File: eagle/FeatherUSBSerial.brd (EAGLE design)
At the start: 50.8 x 22.9 mm, 14 parts, among them U1 FT232RLSSOP

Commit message: Added Big Buttons
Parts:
- added U$3, U$4: TL3300CFXXXQ, S2JLibrary:12MM_TACTILE
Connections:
- new net !RST: MS1.1, U$4.1, U$4.2
- new net MD: MS1.3, U$3.1, U$3.2
- net GND: now also U$3.3, U$3.4, U$4.3, U$4.4
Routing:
- net !RST: track 0.00 -> 52.5 mm, vias 0 -> 2
- net MD: track 0.00 -> 36.3 mm, vias 0 -> 2
- net RX: track 38.1 -> 45.1 mm
- net TX: track 38.0 -> 41.2 mm
- net VCCIO: track 25.6 -> 26.6 mm
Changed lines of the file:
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@@
 <?xml version="1.0" encoding="utf-8"?>
 <!DOCTYPE eagle SYSTEM "eagle.dtd">
-<eagle version="9.2.2">
+<eagle version="9.3.0">
 <drawing>
 <settings>
@@
 <setting verticaltext="up"/>
 </settings>
-<grid distance="0.1" unitdist="inch" unit="inch" style="lines" multiple="1" display="no" altdistance="0.025" altunitdist="inch" altunit="inch"/>
+<grid distance="25" unitdist="mil" unit="mil" style="lines" multiple="1" display="yes" altdistance="12.5" altunitdist="mil" altunit="mil"/>
 <layers>
 <layer number="1" name="Top" color="4" fill="1" visible="yes" active="yes"/>
@@
 <text x="43.815" y="19.431" size="0.8128" layer="21" font="vector" ratio="12">SDA</text>
 <text x="41.021" y="19.431" size="0.8128" layer="21" font="vector" ratio="12">SCL</text>
-<text x="41.2115" y="2.8575" size="0.8128" layer="21" font="vector" ratio="12">TX</text>
+<text x="41.2115" y="2.8575" size="0.7874" layer="21" font="vector" ratio="12">TX</text>
 <text x="38.862" y="2.8575" size="0.8128" layer="21" font="vector" ratio="12">RX</text>
 <text x="36.322" y="2.8575" size="0.8128" layer="21" font="vector" ratio="12">MI</text>
-<text x="33.655" y="2.8575" size="0.8128" layer="21" font="vector" ratio="12">MO</text>
-<text x="30.9118" y="2.8448" size="0.8128" layer="21" font="vector" ratio="12">SCK</text>
+<text x="33.655" y="2.8575" size="0.7874" layer="21" font="vector" ratio="12">MO</text>
+<text x="30.9118" y="2.8448" size="0.7874" layer="21" font="vector" ratio="12">SCK</text>
 <wire x1="2.54" y1="22.86" x2="48.26" y2="22.86" width="0" layer="20"/>
 <wire x1="48.26" y1="22.86" x2="50.8" y2="20.32" width="0" layer="20" curve="-90"/>
@@
 <text x="23.6982" y="2.8448" size="0.8128" layer="21" font="vector" ratio="12">A3</text>
 <text x="26.2382" y="2.8448" size="0.8128" layer="21" font="vector" ratio="12">A4</text>
-<text x="28.7782" y="2.8448" size="0.8128" layer="21" font="vector" ratio="12">A5</text>
+<text x="28.7782" y="2.8448" size="0.7874" layer="21" font="vector" ratio="12">A5</text>
 <text x="23.7744" y="19.431" size="0.8128" layer="21" font="vector" ratio="12">D8</text>
 <text x="26.3144" y="19.431" size="0.8128" layer="21" font="vector" ratio="12">D7</text>
@@
 <attribute name="VALUE" x="22.733" y="11.811" size="0.4064" layer="51" rot="R270"/>
 </element>
+<element name="U$3" library="S2JLibrary" package="12MM_TACTILE" value="TL3300CFXXXQ" x="31.115" y="11.43" smashed="yes" rot="R90">
+<attribute name="DIGI_KEY" value="EG4904CT-ND" x="31.115" y="11.43" size="1.778" layer="27" rot="R90" display="off"/>
+<attribute name="MPN" value="TL3300CF160Q" x="31.115" y="11.43" size="1.778" layer="27" rot="R90" display="off"/>
+<attribute name="NAME" x="24.765" y="6.35" size="1.778" layer="25" rot="R90"/>
+</element>
+<element name="U$4" library="S2JLibrary" package="12MM_TACTILE" value="TL3300CFXXXQ" x="43.815" y="11.43" smashed="yes" rot="R90">
+<attribute name="DIGI_KEY" value="EG4904CT-ND" x="43.815" y="11.43" size="1.778" layer="27" rot="R90" display="off"/>
+<attribute name="MPN" value="TL3300CF160Q" x="43.815" y="11.43" size="1.778" layer="27" rot="R90" display="off"/>
+<attribute name="NAME" x="37.465" y="6.35" size="1.778" layer="25" rot="R90"/>
+</element>
 </elements>
 <signals>
@@
 <via x="9.525" y="17.145" extent="1-16" drill="0.3937"/>
 <via x="13.97" y="13.97" extent="1-16" drill="0.3937"/>
+<contactref element="U$3" pad="3"/>
+<contactref element="U$3" pad="4"/>
+<contactref element="U$4" pad="3"/>
+<contactref element="U$4" pad="4"/>
+<via x="35.56" y="4.445" extent="1-16" drill="0.3937"/>
+<via x="35.56" y="18.415" extent="1-16" drill="0.3937"/>
+<via x="44.45" y="18.415" extent="1-16" drill="0.3937"/>
+<via x="48.26" y="5.08" extent="1-16" drill="0.3937"/>
+<via x="11.7475" y="9.8425" extent="1-16" drill="0.3937"/>
 </signal>
 <signal name="USB-D-">
@@
 <contactref element="C1" pad="1"/>
 <wire x1="5.715" y1="6.565" x2="5.715" y2="8.89" width="0.254" layer="1"/>
-<wire x1="5.715" y1="8.89" x2="6.35" y2="9.525" width="0.254" layer="1"/>
+<wire x1="5.715" y1="8.89" x2="7.62" y2="10.795" width="0.254" layer="1"/>
 <wire x1="14.99" y1="15.721" x2="14.99" y2="16.895" width="0.254" layer="1"/>
 <wire x1="14.99" y1="16.895" x2="15.24" y2="17.145" width="0.254" layer="1"/>
 <wire x1="15.24" y1="17.145" x2="16.51" y2="17.145" width="0.254" layer="1"/>
 <wire x1="16.51" y1="17.145" x2="17.145" y2="16.51" width="0.254" layer="1"/>
-<wire x1="17.145" y1="16.51" x2="17.145" y2="10.16" width="0.254" layer="1"/>
-<wire x1="17.145" y1="10.16" x2="16.51" y2="9.525" width="0.254" layer="1"/>
-<wire x1="16.51" y1="9.525" x2="9.525" y2="9.525" width="0.254" layer="1"/>
-<wire x1="9.525" y1="9.525" x2="6.35" y2="9.525" width="0.254" layer="1"/>
+<wire x1="17.145" y1="16.51" x2="17.145" y2="11.43" width="0.254" layer="1"/>
+<wire x1="17.145" y1="11.43" x2="16.51" y2="10.795" width="0.254" layer="1"/>
+<wire x1="16.51" y1="10.795" x2="8.255" y2="10.795" width="0.254" layer="1"/>
+<wire x1="8.255" y1="10.795" x2="7.62" y2="10.795" width="0.254" layer="1"/>
 <wire x1="9.79" y1="8.409" x2="9.79" y2="9.26" width="0.254" layer="1"/>
-<wire x1="9.79" y1="9.26" x2="9.525" y2="9.525" width="0.254" layer="1"/>
+<wire x1="9.79" y1="9.26" x2="8.255" y2="10.795" width="0.254" layer="1"/>
 </signal>
 <signal name="N$10">
@@
 <contactref element="MS1" pad="14"/>
 <contactref element="U1" pad="1"/>
-<wire x1="39.37" y1="4.445" x2="38.735" y2="5.08" width="0.254" layer="1"/>
-<wire x1="39.37" y1="1.27" x2="39.37" y2="4.445" width="0.254" layer="1"/>
-<wire x1="38.735" y1="5.08" x2="15.24" y2="5.08" width="0.254" layer="1"/>
-<wire x1="15.24" y1="5.08" x2="13.97" y2="5.08" width="0.254" layer="1"/>
-<wire x1="13.97" y1="5.08" x2="8.255" y2="5.08" width="0.254" layer="1"/>
-<wire x1="8.255" y1="5.08" x2="7.84" y2="5.495" width="0.254" layer="1"/>
-<wire x1="7.84" y1="5.495" x2="7.84" y2="8.409" width="0.254" layer="1"/>
+<wire x1="40.9575" y1="2.8575" x2="42.85091875" y2="2.8575" width="0.254" layer="1"/>
+<wire x1="43.815" y1="3.82158125" x2="43.815" y2="5.70341875" width="0.254" layer="1"/>
+<wire x1="43.16841875" y1="6.35" x2="8.89" y2="6.35" width="0.254" layer="1"/>
+<wire x1="7.84" y1="7.4" x2="7.84" y2="8.409" width="0.254" layer="1"/>
+<wire x1="39.37" y1="1.27" x2="40.9575" y2="2.8575" width="0.254" layer="1"/>
+<wire x1="42.85091875" y1="2.8575" x2="43.815" y2="3.82158125" width="0.254" layer="1"/>
+<wire x1="43.815" y1="5.70341875" x2="43.16841875" y2="6.35" width="0.254" layer="1"/>
+<wire x1="8.89" y1="6.35" x2="7.84" y2="7.4" width="0.254" layer="1"/>
 </signal>
 <signal name="TX">
 <contactref element="MS1" pad="15"/>
 <contactref element="U1" pad="5"/>
-<wire x1="41.91" y1="1.27" x2="41.91" y2="5.08" width="0.254" layer="1"/>
-<wire x1="41.91" y1="5.08" x2="41.275" y2="5.715" width="0.254" layer="1"/>
-<wire x1="10.795" y1="5.715" x2="10.44" y2="6.07" width="0.254" layer="1"/>
-<wire x1="10.44" y1="6.07" x2="10.44" y2="8.409" width="0.254" layer="1"/>
-<wire x1="41.275" y1="5.715" x2="10.795" y2="5.715" width="0.254" layer="1"/>
+<wire x1="10.44" y1="8.409" x2="10.44" y2="7.34" width="0.254" layer="1"/>
+<wire x1="10.44" y1="7.34" x2="10.795" y2="6.985" width="0.254" layer="1"/>
+<wire x1="10.795" y1="6.985" x2="43.18" y2="6.985" width="0.254" layer="1"/>
+<wire x1="43.18" y1="6.985" x2="44.45" y2="5.715" width="0.254" layer="1"/>
+<wire x1="44.45" y1="5.715" x2="44.45" y2="3.81" width="0.254" layer="1"/>
+<wire x1="44.45" y1="3.81" x2="41.91" y2="1.27" width="0.254" layer="1"/>
 </signal>
 <signal name="5V">
@@
 <wire x1="24.13" y1="13.093" x2="24.13" y2="11.695" width="0.254" layer="1"/>
 </signal>
+<signal name="MD">
+<contactref element="U$3" pad="1"/>
+<contactref element="U$3" pad="2"/>
+<contactref element="MS1" pad="3"/>
+<wire x1="11.43" y1="1.27" x2="11.43" y2="3.81" width="0.254" layer="1"/>
+<wire x1="11.43" y1="3.81" x2="12.7" y2="5.08" width="0.254" layer="1"/>
+<wire x1="27.99" y1="5.08" x2="28.615" y2="4.455" width="0.254" layer="1"/>
+<wire x1="12.7" y1="5.08" x2="26.67" y2="5.08" width="0.254" layer="1"/>
+<wire x1="26.67" y1="5.08" x2="27.99" y2="5.08" width="0.254" layer="1"/>
+<wire x1="28.615" y1="18.405" x2="27.93" y2="18.405" width="0.254" layer="1"/>
+<wire x1="27.93" y1="18.405" x2="26.67" y2="17.145" width="0.254" layer="1"/>
+<wire x1="26.67" y1="17.145" x2="26.67" y2="8.255" width="0.254" layer="1"/>
+<via x="26.67" y="8.255" extent="1-16" drill="0.3937"/>
+<wire x1="26.67" y1="8.255" x2="26.67" y2="4.445" width="0.254" layer="16"/>
+<via x="26.67" y="4.445" extent="1-16" drill="0.3937"/>
+<wire x1="26.67" y1="4.445" x2="26.67" y2="5.08" width="0.254" layer="1"/>
+</signal>
+<signal name="!RST">
+<contactref element="U$4" pad="1"/>
+<contactref element="U$4" pad="2"/>
+<contactref element="MS1" pad="1"/>
+<wire x1="10.795" y1="5.715" x2="39.37" y2="5.715" width="0.254" layer="1"/>
+<wire x1="39.37" y1="5.715" x2="40.055" y2="5.715" width="0.254" layer="1"/>
+<wire x1="40.055" y1="5.715" x2="41.315" y2="4.455" width="0.254" layer="1"/>
+<wire x1="6.35" y1="1.27" x2="10.795" y2="5.715" width="0.254" layer="1"/>
+<wire x1="41.315" y1="18.405" x2="40.63" y2="18.405" width="0.254" layer="1"/>
+<wire x1="40.63" y1="18.405" x2="39.37" y2="17.145" width="0.254" layer="1"/>
+<wire x1="39.37" y1="17.145" x2="39.37" y2="8.255" width="0.254" layer="1"/>
+<via x="39.37" y="8.255" extent="1-16" drill="0.3937"/>
+<wire x1="39.37" y1="8.255" x2="39.37" y2="5.08" width="0.254" layer="16"/>
+<via x="39.37" y="5.08" extent="1-16" drill="0.3937"/>
+<wire x1="39.37" y1="5.08" x2="39.37" y2="5.715" width="0.254" layer="1"/>
+</signal>
 </signals>

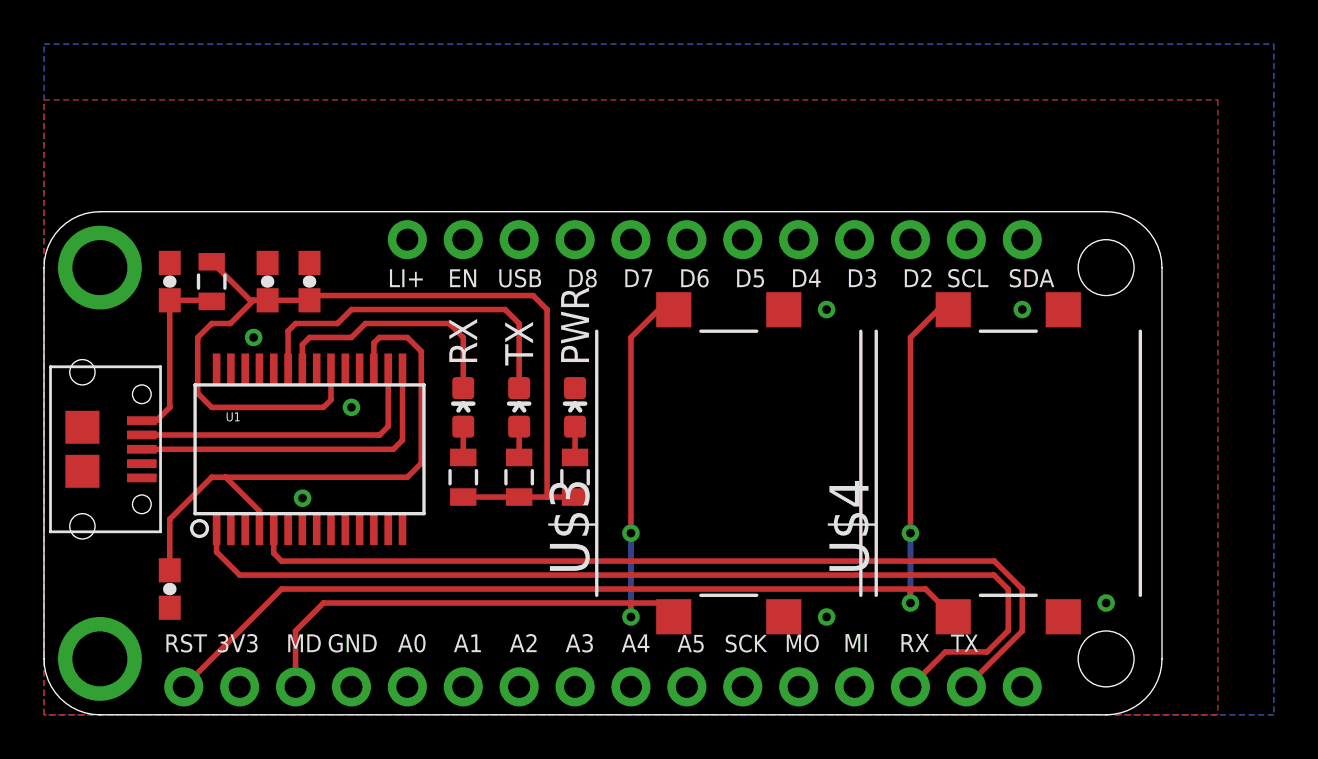
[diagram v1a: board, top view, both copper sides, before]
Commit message: Updated to use more common and easier to manipulate 0805 Cap's and Resistors.
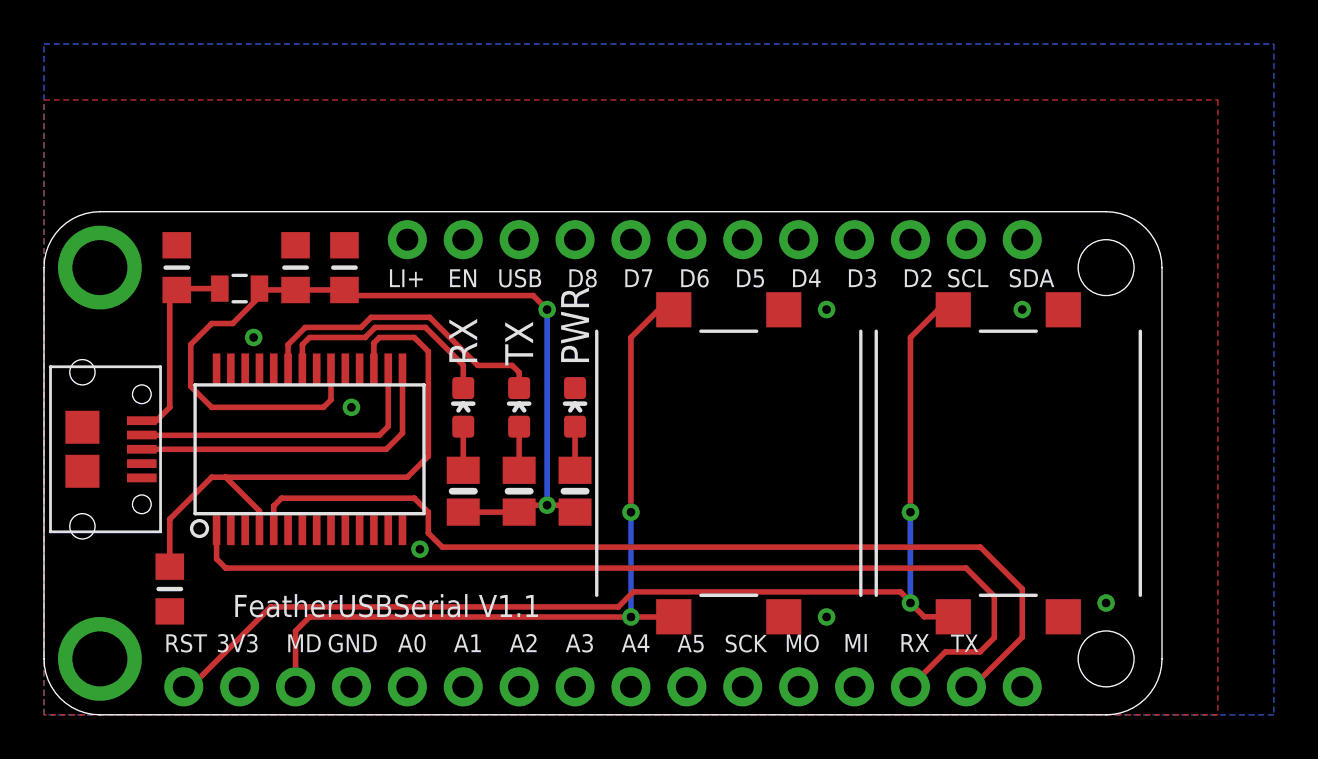
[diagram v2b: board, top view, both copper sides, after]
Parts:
- C1, C2, C3, C4: device rickk2:0603-CAP -> S2JLibrary:_0805MP
- R1, R3, R4: device rickk2:0805 -> S2JLibrary:0805-NO
- moved C4 1.71 mm to (13.7, 20.3)
- moved C3 1.42 mm to (11.4, 20.3)
- moved U$2 1.31 mm to (8.89, 19.4), turned to 0 degrees
- moved C2 0.71 mm to (6.03, 20.3)
- moved R1 0.63 mm to (24.1, 10.2)
- moved R3 0.63 mm to (21.6, 10.2)
- moved R4 0.63 mm to (19.1, 10.2)
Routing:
- net TXLED: track 15.8 -> 13.9 mm
- net TX: track 41.2 -> 43.2 mm
- net 5V: track 43.6 -> 42.4 mm, vias 0 -> 2
- net MD: track 36.3 -> 35.2 mm
- net RX: track 45.1 -> 44.0 mm
- net RXLED: track 11.4 -> 10.5 mm
- net VBUS: track 8.31 -> 9.05 mm
- net !RST: track 52.5 -> 51.8 mm
- net N$5: track 1.40 -> 1.98 mm
- net N$11: track 1.40 -> 1.98 mm
- net N$10: track 1.40 -> 1.98 mm
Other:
- board text added: "FeatherUSBSerial V1.1"
